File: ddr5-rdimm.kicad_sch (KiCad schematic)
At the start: 20 parts, among them J2 Bus_DDR5_DDR504111002KQ, Q10 BSS138PW, Q11 BSS138PW, Q9 BSS138PW, SW3 SW_KMR211NGLFS_SMD

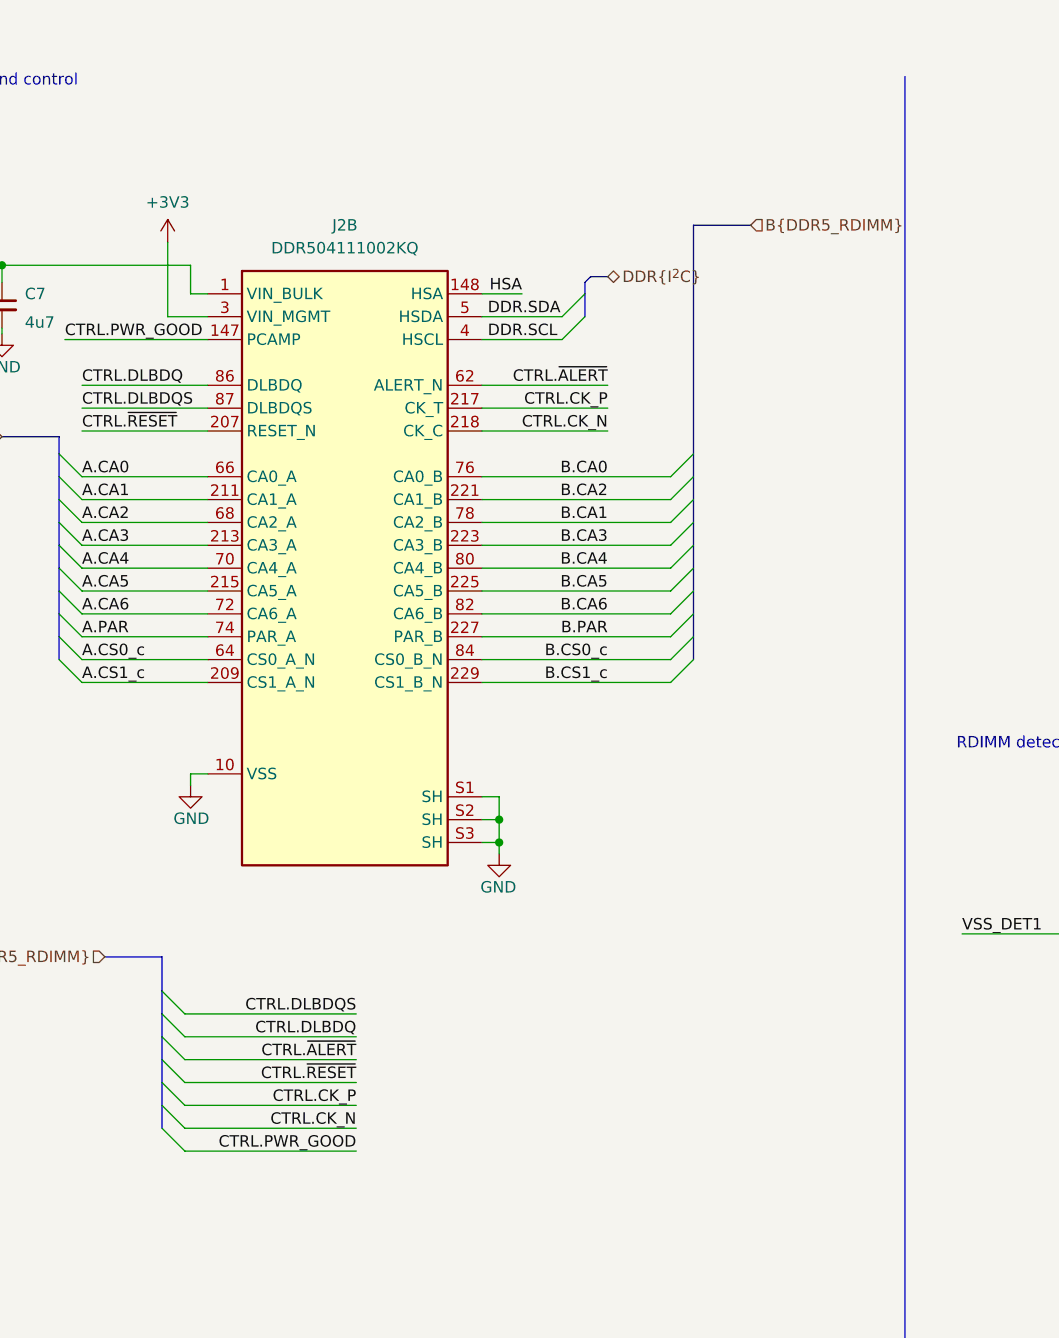
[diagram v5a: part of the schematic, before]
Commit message: [#67402] Connect low speed signals and interfaces to the HD banks
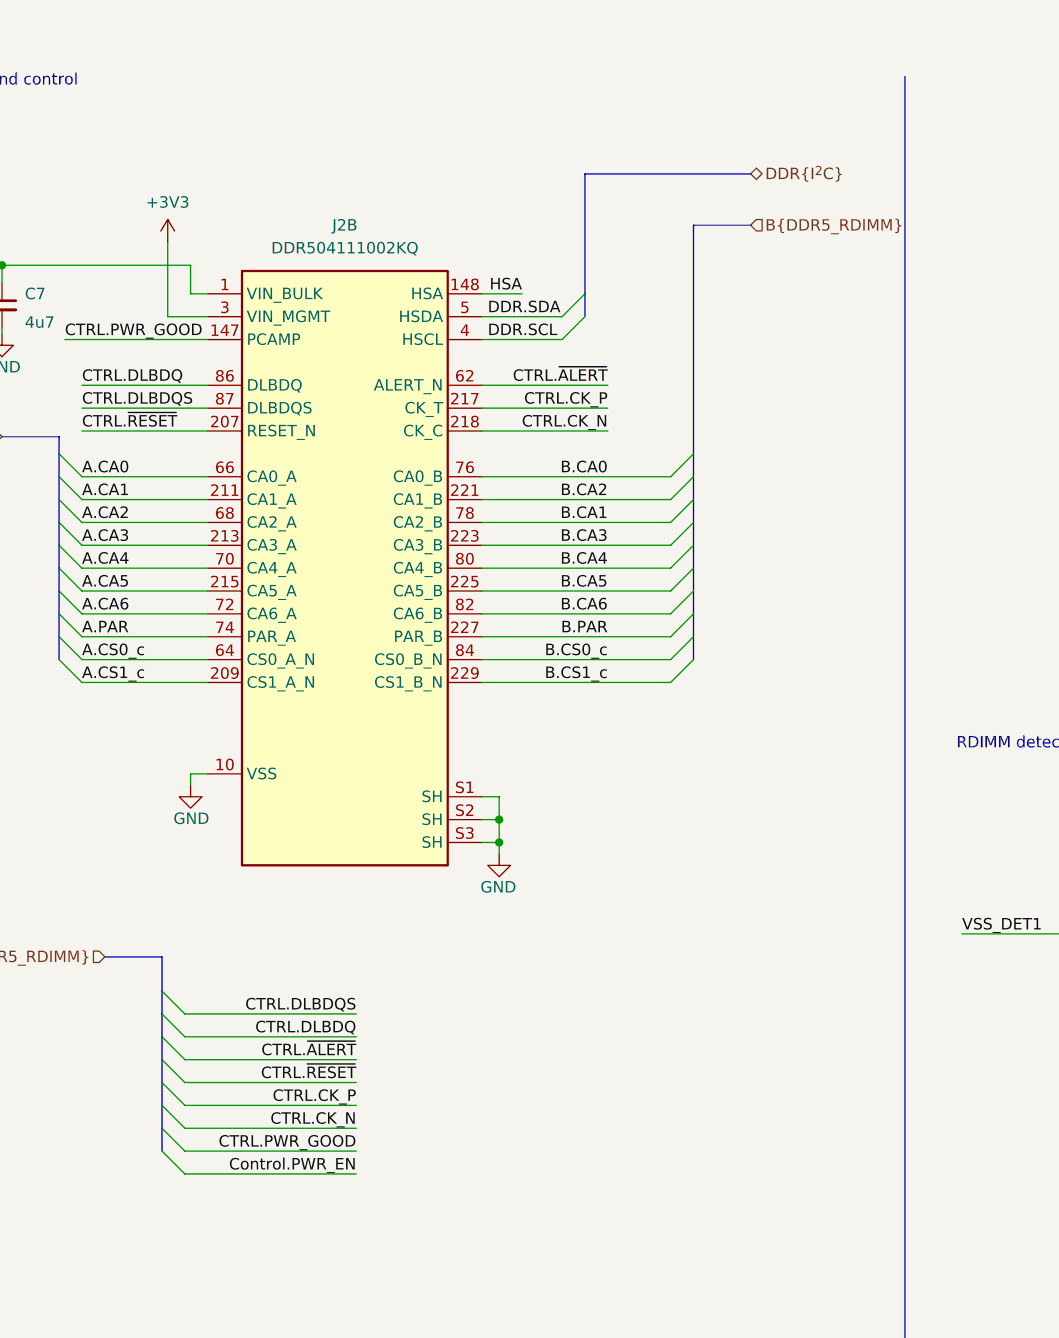
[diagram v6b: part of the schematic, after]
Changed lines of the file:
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@@
     (stroke (width 0) (type default))
   )
+  (bus_entry (at 167.64 147.32) (size -2.54 -2.54)
+    (stroke (width 0) (type default))
+  )
   (bus_entry (at 41.91 193.04) (size -2.54 -2.54)
     (stroke (width 0) (type default))
@@
     (stroke (width 0) (type default))
   )
-  (bus (pts (xy 224.155 41.91) (xy 224.155 67.31))
-    (stroke (width 0) (type default))
-  )
   (wire (pts (xy 137.16 46.355) (xy 147.32 46.355))
     (stroke (width 0) (type default))
@@
     (stroke (width 0) (type default))
   )
+  (bus (pts (xy 165.1 142.24) (xy 165.1 144.78))
+    (stroke (width 0) (type default))
+  )
   (wire (pts (xy 41.91 187.96) (xy 55.88 187.96))
     (stroke (width 0) (type default))
@@
     (stroke (width 0) (type default))
   )
-  (bus (pts (xy 224.155 41.91) (xy 230.505 41.91))
-    (stroke (width 0) (type default))
-  )
   (wire (pts (xy 41.91 106.68) (xy 55.88 106.68))
     (stroke (width 0) (type default))
@@
     (stroke (width 0) (type default))
   )
+  (wire (pts (xy 167.64 147.32) (xy 186.69 147.32))
+    (stroke (width 0) (type default))
+  )
   (bus (pts (xy 39.37 99.06) (xy 39.37 101.6))
     (stroke (width 0) (type default))
@@
     (stroke (width 0) (type default))
   )
+  (bus (pts (xy 212.09 36.195) (xy 230.505 36.195))
+    (stroke (width 0) (type default))
+  )
   (wire (pts (xy 156.21 77.47) (xy 170.18 77.47))
     (stroke (width 0) (type default))
@@
     (stroke (width 0) (type default))
   )
+  (bus (pts (xy 212.09 36.195) (xy 212.09 49.53))
+    (stroke (width 0) (type default))
+  )
   (wire (pts (xy 147.32 46.355) (xy 168.275 46.355))
     (stroke (width 0) (type default))
@@
     (stroke (width 0) (type default))
   )
+  (bus (pts (xy 224.155 41.91) (xy 230.505 41.91))
+    (stroke (width 0) (type default))
+  )
   (bus (pts (xy 165.1 127) (xy 165.1 129.54))
     (stroke (width 0) (type default))
@@
     (stroke (width 0) (type default))
   )
-  (bus (pts (xy 214.63 47.625) (xy 212.725 47.625))
-    (stroke (width 0) (type default))
-  )
   (bus (pts (xy 102.87 139.7) (xy 102.87 144.78))
     (stroke (width 0) (type default))
@@
     (stroke (width 0) (type default))
   )
-  (bus (pts (xy 212.09 48.26) (xy 212.09 49.53))
-    (stroke (width 0) (type default))
-  )
   (wire (pts (xy 156.21 64.77) (xy 170.18 64.77))
     (stroke (width 0) (type default))
@@
     (stroke (width 0) (type default))
   )
+  (bus (pts (xy 224.155 41.91) (xy 224.155 67.31))
+    (stroke (width 0) (type default))
+  )
   (bus (pts (xy 102.87 182.88) (xy 102.87 185.42))
     (stroke (width 0) (type default))
@@
     (stroke (width 0) (type default))
   )
-  (bus (pts (xy 212.725 47.625) (xy 212.09 48.26))
-    (stroke (width 0) (type default))
-  )
   (wire (pts (xy 86.36 180.34) (xy 100.33 180.34))
     (stroke (width 0) (type default))
@@
     (effects (font (size 1.27 1.27)) (justify right bottom))
   )
+  (label "Control.PWR_EN" (at 186.69 147.32 180) (fields_autoplaced)
+    (effects (font (size 1.27 1.27)) (justify right bottom))
+  )
   (label "B.DQS3_P" (at 100.33 157.48 180) (fields_autoplaced)
     (effects (font (size 1.27 1.27)) (justify right bottom))
@@
     )
   )
-  (hierarchical_label "DDR{I^{2}C}" (shape bidirectional) (at 214.63 47.625 0) (fields_autoplaced)
+  (hierarchical_label "DDR{I^{2}C}" (shape bidirectional) (at 230.505 36.195 0) (fields_autoplaced)
     (effects (font (size 1.27 1.27)) (justify left))
   )

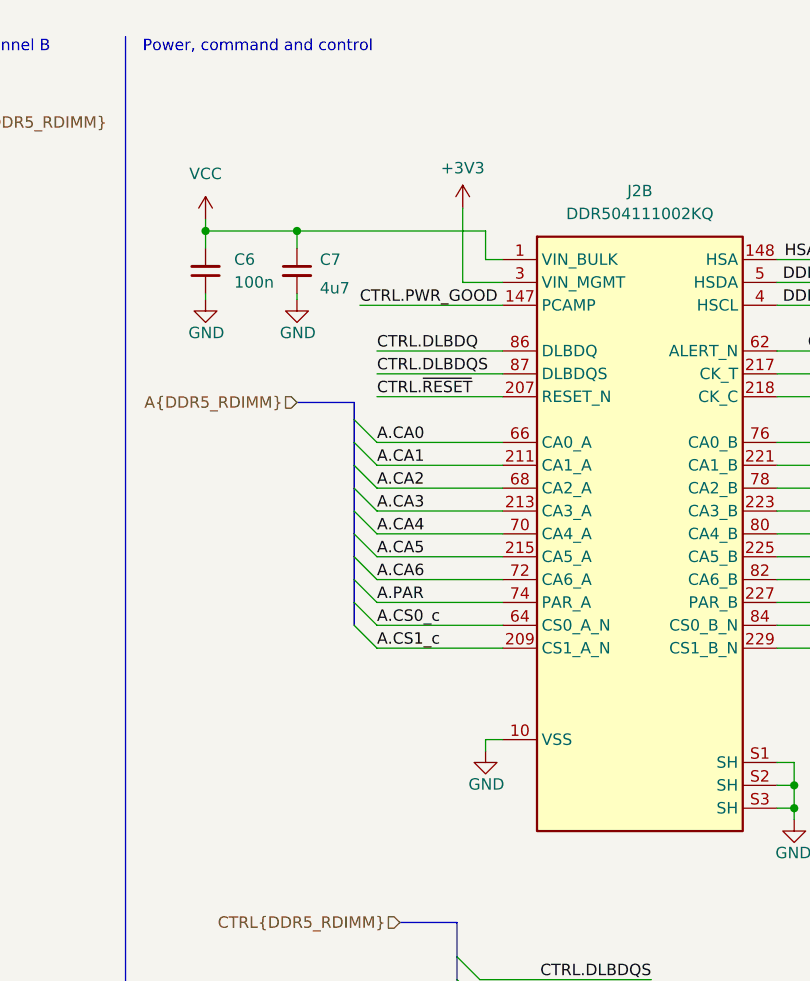
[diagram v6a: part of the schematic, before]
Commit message: [#66727] Minor schematic improvements. Finish routing right side of the board
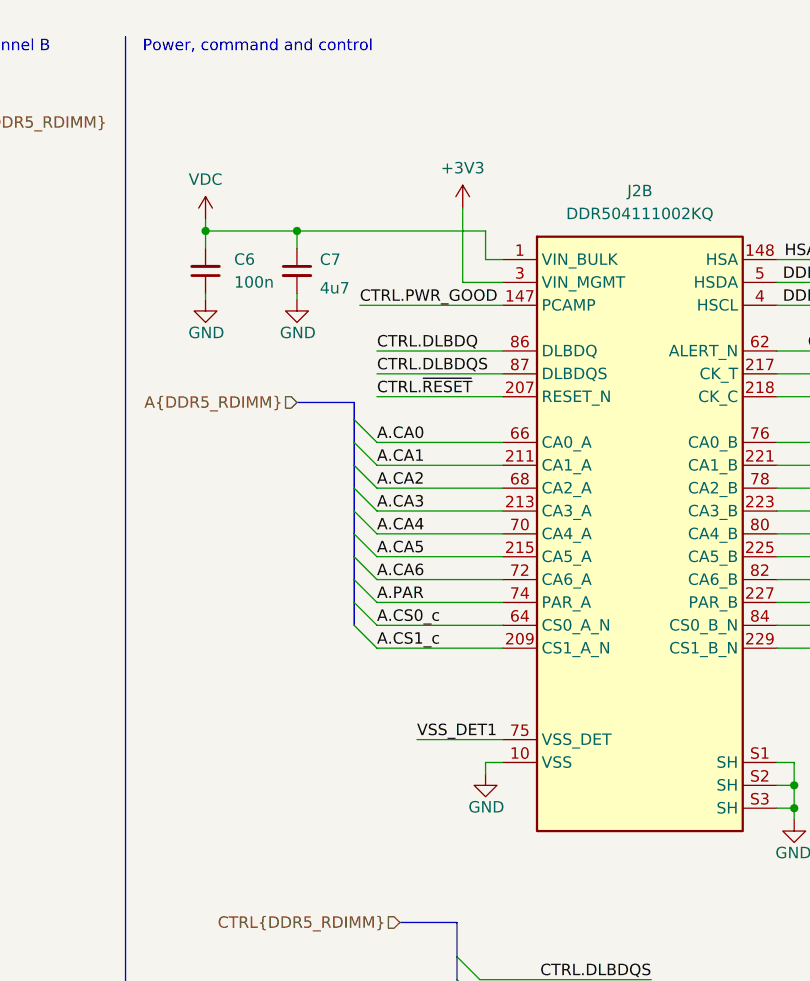
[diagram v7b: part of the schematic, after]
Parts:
- J2: symbol antmicroMemoryConnectorsPCCardSockets:Bus_DDR5_DDR504111002KQ -> antmicroMemoryConnectorsPCCardSockets:Bus_DDR5_DDR504111002KQ_CUSTOM_1xDetectPin
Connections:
- net GND: no longer J2.75 (VSS)
- net VSS_DET1: now also J2.75 (VSS_DET)
- net VCC renamed VDC
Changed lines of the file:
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@@
     (stroke (width 0) (type default))
   )
-  (wire (pts (xy 168.275 102.87) (xy 170.18 102.87))
+  (wire (pts (xy 168.275 105.41) (xy 170.18 105.41))
     (stroke (width 0) (type default))
   )
@@
     (stroke (width 0) (type default))
   )
+  (wire (pts (xy 160.655 102.87) (xy 170.18 102.87))
+    (stroke (width 0) (type default))
+  )
   (bus (pts (xy 39.37 124.46) (xy 39.37 127))
     (stroke (width 0) (type default))
@@
     (stroke (width 0) (type default))
   )
-  (wire (pts (xy 168.275 104.14) (xy 168.275 102.87))
+  (wire (pts (xy 168.275 106.68) (xy 168.275 105.41))
     (stroke (width 0) (type default))
   )
@@
     (effects (font (size 1.27 1.27)) (justify right bottom))
   )
+  (label "VSS_DET1" (at 160.655 102.87 0) (fields_autoplaced)
+    (effects (font (size 1.27 1.27)) (justify left bottom))
+  )
   (label "B.DQ10" (at 100.33 86.36 180) (fields_autoplaced)
     (effects (font (size 1.27 1.27)) (justify right bottom))
@@
     )
   )
+  (symbol (lib_id "antmicropower:VDC") (at 137.16 45.085 0) (unit 1)
+    (in_bom yes) (on_board yes) (dnp no) (fields_autoplaced)
+    (property "Reference" "#PWR033" (at 137.16 47.625 0)
+      (effects (font (size 1.27 1.27)) hide)
+    )
+    (property "Value" "VDC" (at 137.16 40.64 0)
+      (effects (font (size 1.27 1.27)))
+    )
+    (property "Footprint" "" (at 137.16 45.085 0)
+      (effects (font (size 1.27 1.27)) hide)
+    )
+    (property "Datasheet" "" (at 137.16 45.085 0)
+      (effects (font (size 1.27 1.27)) hide)
+    )
+    (pin "1")
+    (instances
+      (project "data-center-rdimm-ddr5-tester"
+        (path "/1faa6543-e26a-4449-8bac-ee14b9f19e5f/00000000-0000-0000-0000-000061827943"
+          (reference "#PWR033") (unit 1)
+        )
+      )
+    )
+  )
   (symbol (lib_id "antmicroResistors0402:R_47k_0402") (at 271.78 116.205 90) (unit 1)
     (in_bom yes) (on_board yes) (dnp no) (fields_autoplaced)
@@
     )
   )
-  (symbol (lib_id "antmicropower:VCC") (at 137.16 45.085 0) (unit 1)
-    (in_bom yes) (on_board yes) (dnp no) (fields_autoplaced)
-    (property "Reference" "#PWR033" (at 137.16 48.895 0)
-      (effects (font (size 1.27 1.27)) hide)
-    )
-    (property "Value" "VCC" (at 137.16 40.005 0)
-      (effects (font (size 1.27 1.27)))
-    )
-    (property "Footprint" "" (at 137.16 45.085 0)
-      (effects (font (size 1.27 1.27)) hide)
-    )
-    (property "Datasheet" "" (at 137.16 45.085 0)
-      (effects (font (size 1.27 1.27)) hide)
-    )
-    (pin "1")
-    (instances
-      (project "data-center-rdimm-ddr5-tester"
-        (path "/1faa6543-e26a-4449-8bac-ee14b9f19e5f/00000000-0000-0000-0000-000061827943"
-          (reference "#PWR033") (unit 1)
-        )
-      )
-    )
-  )
   (symbol (lib_id "antmicroResistors0402:R_330R_0402") (at 205.74 210.82 270) (unit 1)
     (in_bom yes) (on_board yes) (dnp no) (fields_autoplaced)
@@
     )
   )
-  (symbol (lib_id "antmicropower:GND") (at 168.275 104.14 0) (unit 1)
+  (symbol (lib_id "antmicropower:GND") (at 168.275 106.68 0) (unit 1)
     (in_bom yes) (on_board yes) (dnp no) (fields_autoplaced)
-    (property "Reference" "#PWR038" (at 168.275 110.49 0)
+    (property "Reference" "#PWR038" (at 168.275 113.03 0)
       (effects (font (size 1.27 1.27)) hide)
     )
-    (property "Value" "GND" (at 166.37 108.585 0)
+    (property "Value" "GND" (at 166.37 111.125 0)
       (effects (font (size 1.27 1.27) (thickness 0.15)) (justify left bottom))
     )
-    (property "Footprint" "" (at 177.165 111.76 0)
+    (property "Footprint" "" (at 177.165 114.3 0)
       (effects (font (size 1.27 1.27) (thickness 0.15)) (justify left bottom) hide)
     )
-    (property "Datasheet" "" (at 177.165 116.84 0)
+    (property "Datasheet" "" (at 177.165 119.38 0)
       (effects (font (size 1.27 1.27) (thickness 0.15)) (justify left bottom) hide)
     )
-    (property "Author" "Antmicro" (at 177.165 109.22 0)
+    (property "Author" "Antmicro" (at 177.165 111.76 0)
       (effects (font (size 1.27 1.27) (thickness 0.15)) (justify left bottom) hide)
     )
-    (property "License" "Apache-2.0" (at 177.165 111.76 0)
+    (property "License" "Apache-2.0" (at 177.165 114.3 0)
       (effects (font (size 1.27 1.27) (thickness 0.15)) (justify left bottom) hide)
     )
@@
     )
   )
-  (symbol (lib_id "antmicroMemoryConnectorsPCCardSockets:Bus_DDR5_DDR504111002KQ") (at 170.18 49.53 0) (unit 2)
+  (symbol (lib_id "antmicroMemoryConnectorsPCCardSockets:Bus_DDR5_DDR504111002KQ_CUSTOM_1xDetectPin") (at 170.18 49.53 0) (unit 2)
     (in_bom yes) (on_board yes) (dnp no) (fields_autoplaced)
     (property "Reference" "J2" (at 185.42 41.91 0)

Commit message: [#67725] Update DDR5 RDIMM
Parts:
- removed D9: LED_RGY_0606_APTF1616SURKCGKSYKC, antmicro-footprints:LED_RGY_1.6x1.6mm_APTF1616, symbol antmicroLEDIndicationDiscrete:LED_RGY_0606_APTF1616SURKCGKSYKC
- added D20: LED_RGY_0606_APTF1616SURKCGKSYKC, antmicro-footprints:LED_RGY_1.6x1.6mm_APTF1616, symbol antmicroLEDIndicationDiscrete:LED_RGY_0606_APTF1616SURKCGKSYKC
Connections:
- net +3V3: now also D20.1 (A)
- net at R63.1: now also D20.2 (C_{R})
- net at R62.1: now also D20.3 (C_{G})
- net at R61.1: now also D20.4 (C_{Y})
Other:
- moved on the sheet: C10, C127, C6, C7, C8, C9, J2A, J2B, Q10, Q11, Q9, R128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
